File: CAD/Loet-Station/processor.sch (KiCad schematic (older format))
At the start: 0 parts

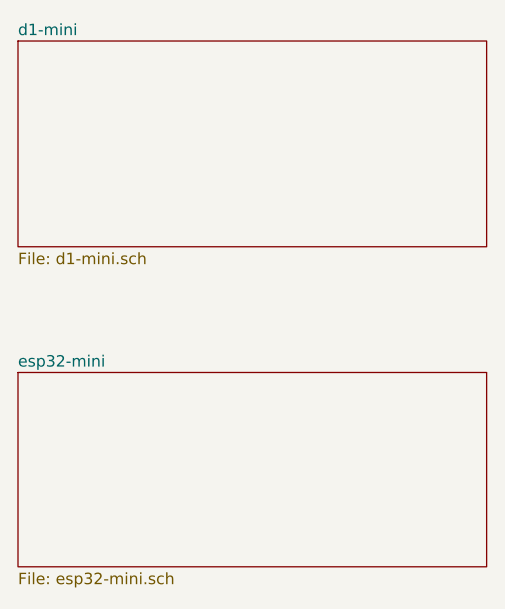
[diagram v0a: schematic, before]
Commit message: changed d1 mini pins, optional i2c oled
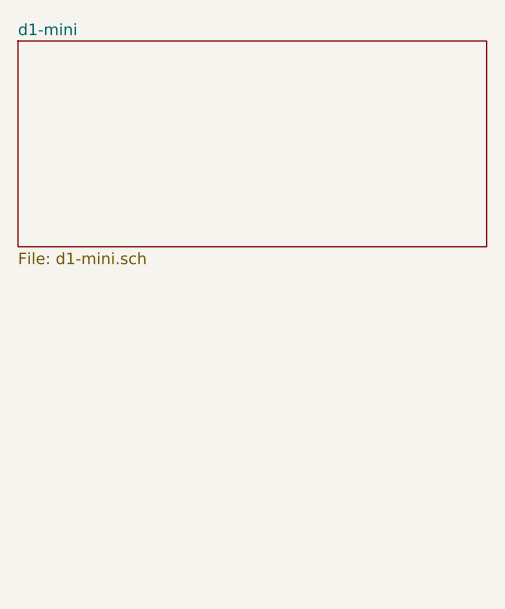
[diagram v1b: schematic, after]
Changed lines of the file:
@@
 $Descr A4 11693 8268
 encoding utf-8
-Sheet 2 7
+Sheet 2 6
 Title ""
 Date ""
@@
 F1 "d1-mini.sch" 50
 $EndSheet
-$Sheet
-S 6850 2500 2050 850
-U 6039CA1A
-F0 "esp32-mini" 50
-F1 "esp32-mini.sch" 50
-$EndSheet
 $EndSCHEMATC

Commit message: esp32-mini added, pwm driver for 24v
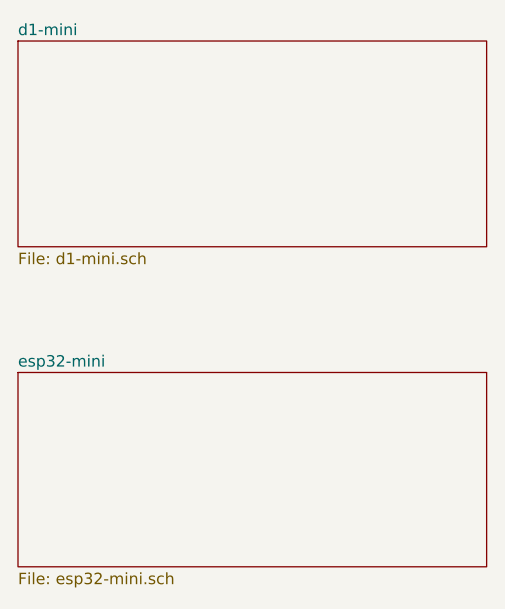
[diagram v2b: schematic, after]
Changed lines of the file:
@@
 $Descr A4 11693 8268
 encoding utf-8
-Sheet 2 6
+Sheet 2 7
 Title ""
 Date ""
@@
 F1 "d1-mini.sch" 50
 $EndSheet
+$Sheet
+S 6850 2500 2050 850
+U 6039CA1A
+F0 "esp32-mini" 50
+F1 "esp32-mini.sch" 50
+$EndSheet
 $EndSCHEMATC
